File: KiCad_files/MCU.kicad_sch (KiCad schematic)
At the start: 9 parts, among them U1 B3U-1000P, U12 ESP32-S3-MINI-1U

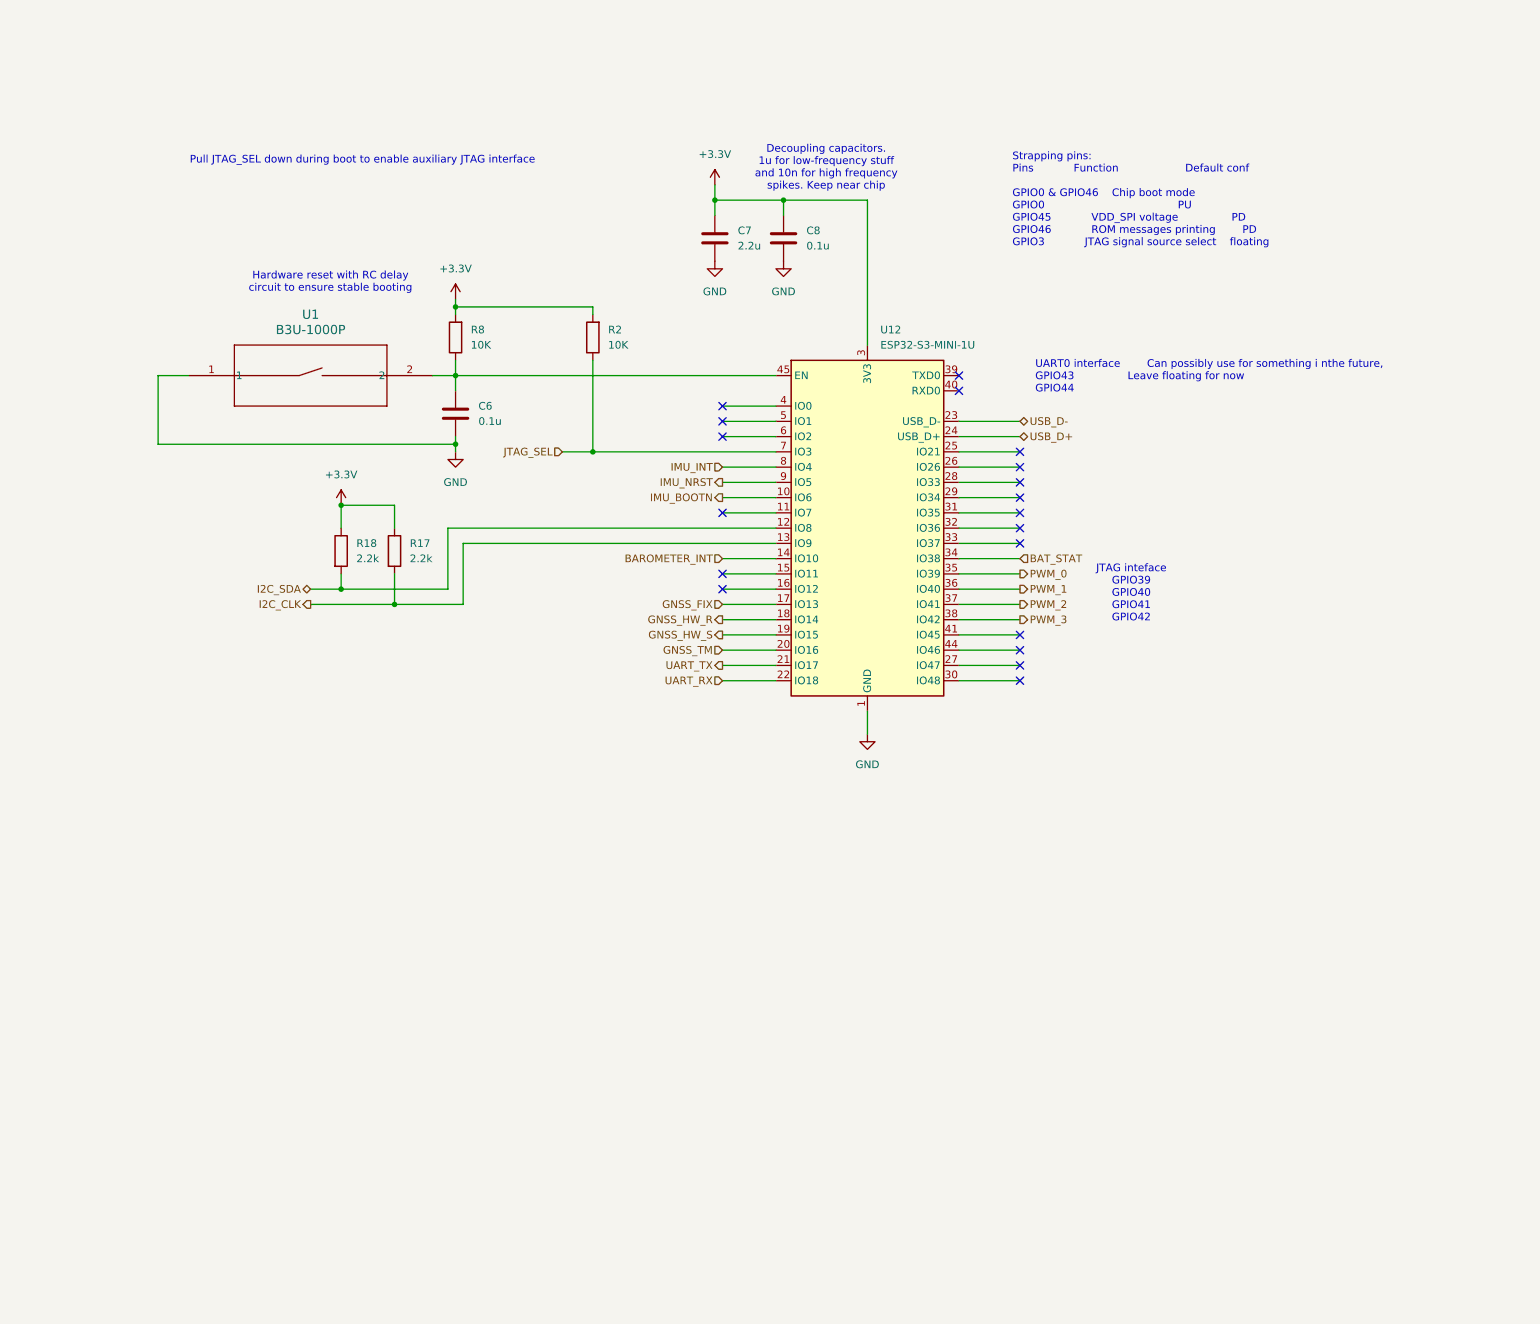
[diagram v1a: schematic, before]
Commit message: headerit mietitty, pinnijärjestystä muutettu mcussa
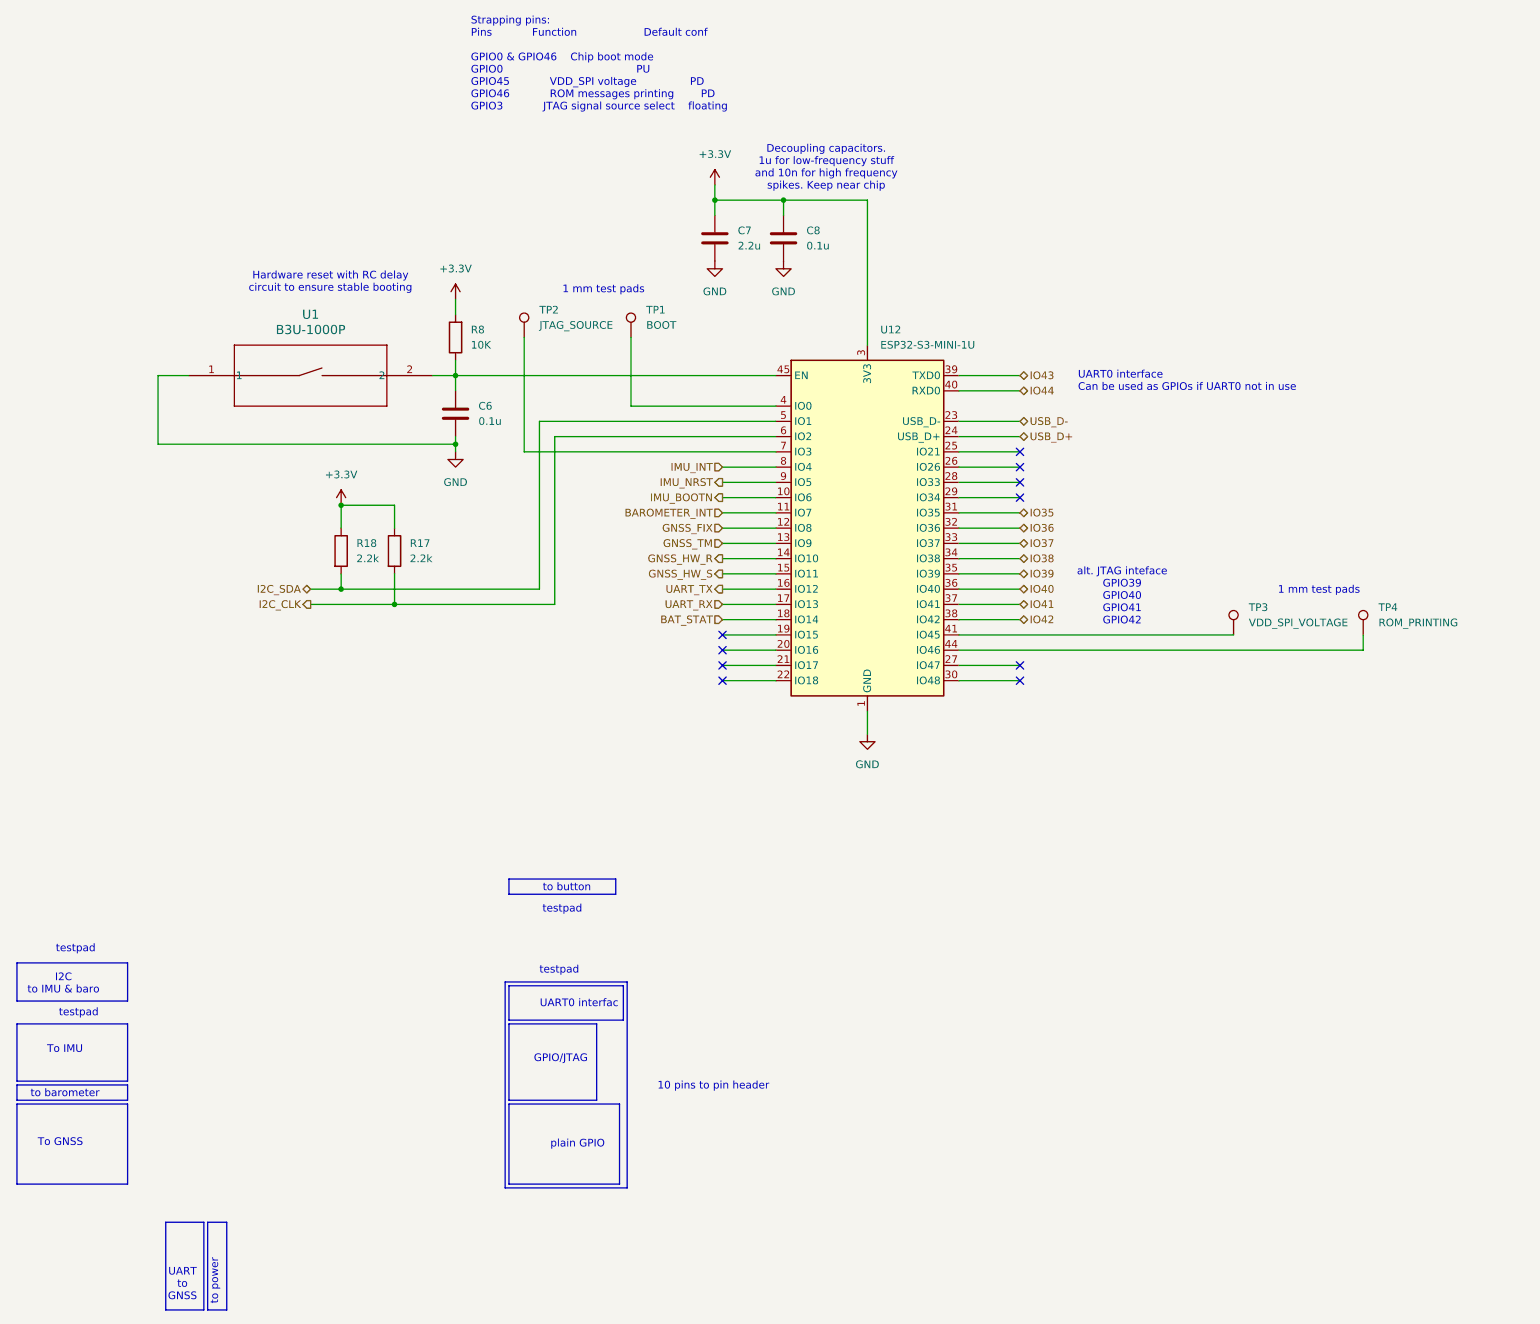
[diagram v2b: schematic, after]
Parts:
- removed R2: 10K, Resistor_SMD:R_0805_2012Metric_Pad1.20x1.40mm_HandSolder, symbol Device:R
- added TP1: BOOT, TestPoint:TestPoint_Pad_D1.0mm, symbol Connector:TestPoint
- added TP2: JTAG_SOURCE, TestPoint:TestPoint_Pad_D1.0mm, symbol Connector:TestPoint
- added TP3: VDD_SPI_VOLTAGE, TestPoint:TestPoint_Pad_D1.0mm, symbol Connector:TestPoint
- added TP4: ROM_PRINTING, TestPoint:TestPoint_Pad_D1.0mm, symbol Connector:TestPoint
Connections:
- net BAROMETER_INT: now also U12.11 (IO7); no longer U12.14 (IO10)
- net BAT_STAT: now also U12.18 (IO14); no longer U12.34 (IO38)
- net GNSS_FIX: now also U12.12 (IO8); no longer U12.17 (IO13)
- net GNSS_HW_R: now also U12.14 (IO10); no longer U12.18 (IO14)
- net GNSS_HW_S: now also U12.15 (IO11); no longer U12.19 (IO15)
- net GNSS_TM: now also U12.13 (IO9); no longer U12.20 (IO16)
- net I2C_CLK: now also U12.6 (IO2); no longer U12.13 (IO9)
- net I2C_SDA: now also U12.5 (IO1); no longer U12.12 (IO8)
- net UART_RX: now also U12.17 (IO13); no longer U12.22 (IO18)
- net UART_TX: now also U12.16 (IO12); no longer U12.21 (IO17)
- net IO35: now reaches U12.31 (IO35)
- net IO36: now reaches U12.32 (IO36)
- net IO37: now reaches U12.33 (IO37)
- net IO43: now reaches U12.39 (TXD0)
- net at U12.4 (IO0): now also TP1.1
- net IO44: now reaches U12.40 (RXD0)
- net at U12.41 (IO45): now also TP3.1
- net at U12.44 (IO46): now also TP4.1
- net JTAG_SEL: no longer names the net of U12.7 (IO3)
- net JTAG_SEL: now also TP2.1
- net PWM_0 renamed IO39
- net PWM_1 renamed IO40
- net PWM_2 renamed IO41
- net PWM_3 renamed IO42
- new net IO38: U12.34 (IO38)
- no-connect marks 19 -> 10
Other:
- note added: "1 mm test pads"
- note added: "10 pins to pin header"
- note added: "GPIO/JTAG"
- note added: "I2C to IMU & baro"
- note added: "To GNSS"
- note added: "To IMU"
- note added: "UART to GNSS"
- note added: "UART0 interfac"
- note added: "UART0 interface Can be used as GPIOs if UART0 not in use"
- note added: "alt. JTAG inteface GPIO39 GPIO40 GPIO41 GPIO42"
- note added: "plain GPIO"
- note added: "testpad"
- note added: "to barometer"
- note added: "to button"
- note added: "to power"
- note removed: "JTAG inteface GPIO39 GPIO40 GPIO41 GPIO42"
- note removed: "Pull JTAG_SEL down during boot to enable auxiliary JTAG interface"
- note removed: "UART0 interface Can possibly use for something i nthe future, GPIO43 Leave floating for now GPIO44"

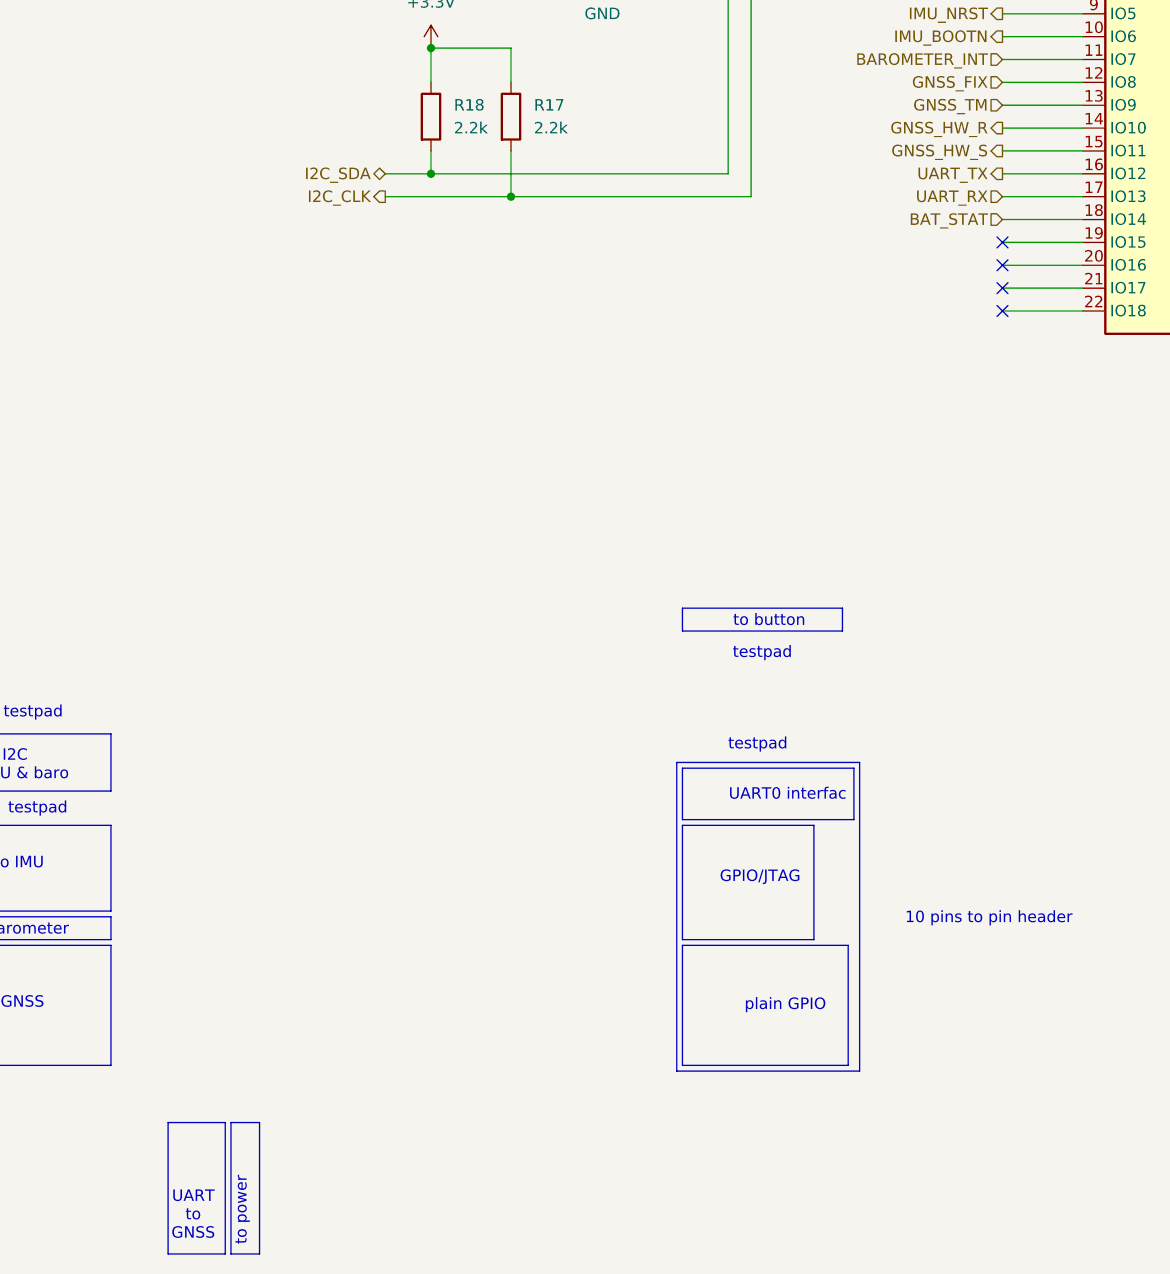
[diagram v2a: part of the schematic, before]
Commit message: UART1 siirretty parempaan paikkaan
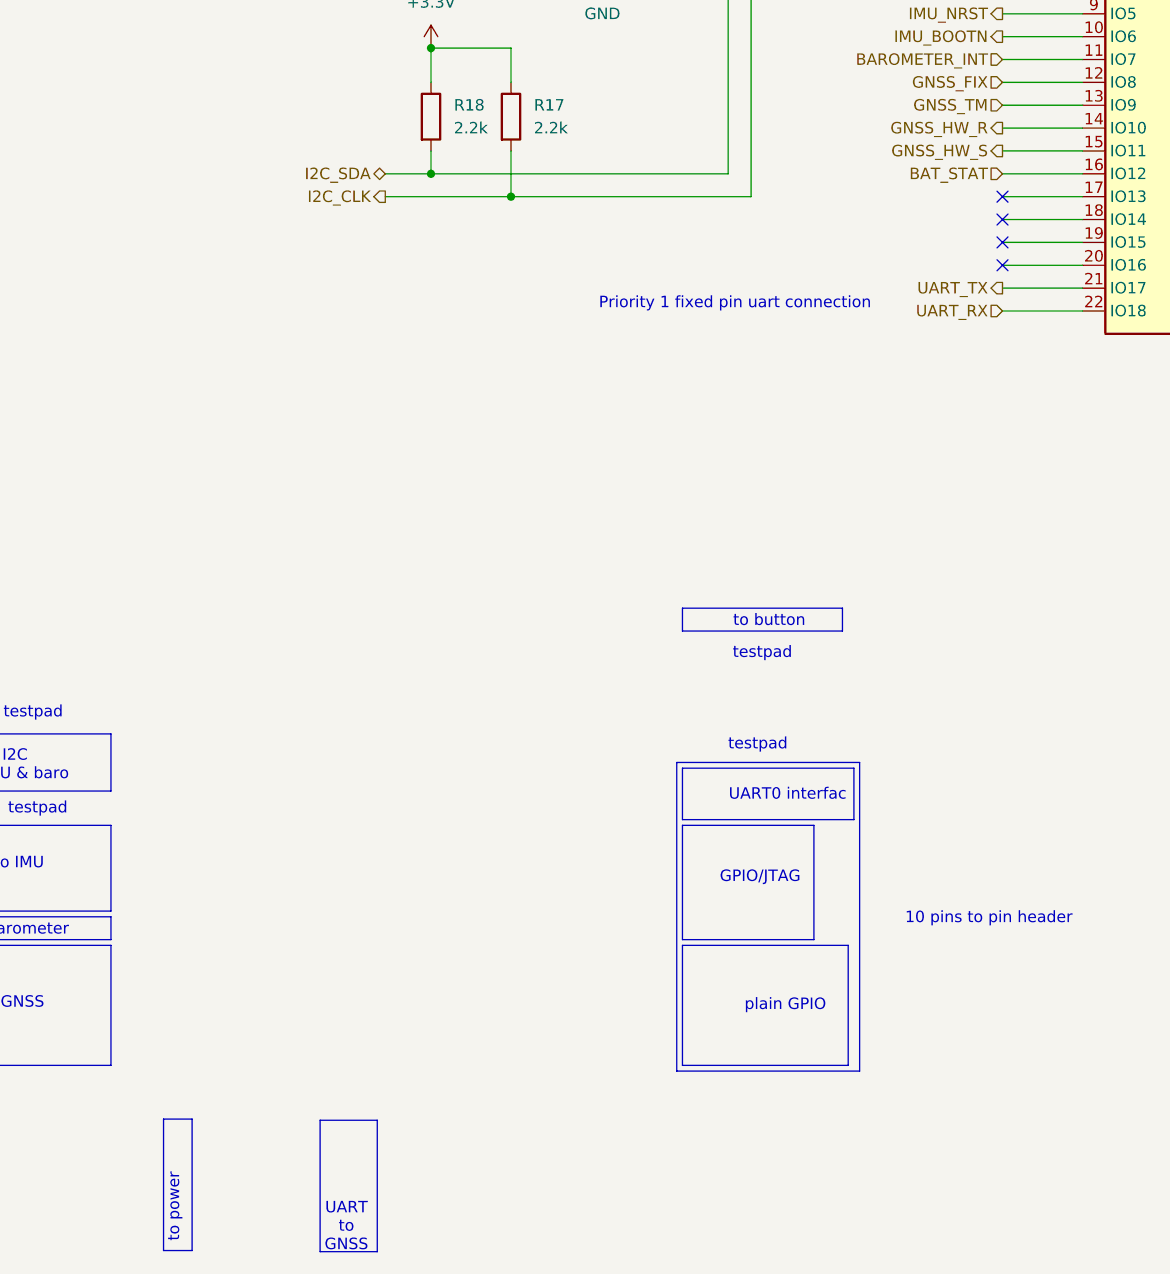
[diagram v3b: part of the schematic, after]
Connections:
- net BAT_STAT: now also U12.16 (IO12); no longer U12.18 (IO14)
- net UART_RX: now also U12.22 (IO18); no longer U12.17 (IO13)
- net UART_TX: now also U12.21 (IO17); no longer U12.16 (IO12)
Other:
- note added: "Priority 1 fixed pin uart connection"
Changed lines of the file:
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@@
 	)
 	(rectangle
-		(start 59.055 220.98)
-		(end 62.23 235.585)
+		(start 51.562 220.599)
+		(end 54.737 235.204)
 		(stroke
 			(width 0)
@@
 	)
 	(rectangle
-		(start 52.07 220.98)
-		(end 58.42 235.585)
+		(start 68.961 220.726)
+		(end 75.311 235.331)
 		(stroke
 			(width 0)
@@
 		)
 	)
+	(text "Priority 1 fixed pin uart connection"
+		(exclude_from_sim no)
+		(at 115.062 130.048 0)
+		(effects
+			(font
+				(size 1.27 1.27)
+			)
+		)
+	)
 	(text "1 mm test pads"
 		(exclude_from_sim no)
@@
 	(text "to power"
 		(exclude_from_sim no)
-		(at 60.198 230.886 90)
+		(at 52.705 230.505 90)
 		(effects
 			(font
@@
 	(text "UART\nto\nGNSS"
 		(exclude_from_sim no)
-		(at 54.864 231.394 0)
+		(at 71.882 232.664 0)
 		(effects
 			(font
@@
 	)
 	(no_connect
-		(at 144.78 123.19)
-	)
-	(no_connect
-		(at 144.78 128.27)
+		(at 144.78 120.65)
 	)
 	(no_connect
@@
 	)
 	(no_connect
+		(at 144.78 123.19)
+	)
+	(no_connect
 		(at 194.31 100.33)
 	)
@@
 	)
 	(no_connect
-		(at 144.78 130.81)
+		(at 144.78 118.11)
 	)
 	(no_connect
@@
 		)
 	)
-	(hierarchical_label "BAT_STAT"
-		(shape input)
-		(at 144.78 120.65 180)
-		(effects
-			(font
-				(size 1.27 1.27)
-			)
-			(justify right)
-		)
-	)
 	(hierarchical_label "GNSS_HW_R"
 		(shape output)
@@
 		)
 	)
+	(hierarchical_label "UART_RX"
+		(shape input)
+		(at 144.78 130.81 180)
+		(effects
+			(font
+				(size 1.27 1.27)
+			)
+			(justify right)
+		)
+	)
 	(hierarchical_label "GNSS_TM"
 		(shape input)
@@
 		)
 	)
-	(hierarchical_label "UART_TX"
-		(shape output)
+	(hierarchical_label "BAT_STAT"
+		(shape input)
 		(at 144.78 115.57 180)
-		(effects
-			(font
-				(size 1.27 1.27)
-			)
-			(justify right)
-		)
-	)
-	(hierarchical_label "UART_RX"
-		(shape input)
-		(at 144.78 118.11 180)
 		(effects
 			(font
@@
 		)
 	)
+	(hierarchical_label "UART_TX"
+		(shape output)
+		(at 144.78 128.27 180)
+		(effects
+			(font
+				(size 1.27 1.27)
+			)
+			(justify right)
+		)
+	)

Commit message: gepsiä alotettu
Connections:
- net BAT_STAT: now also U12.30 (IO48); no longer U12.16 (IO12)
- net GNSS_FIX: now also U12.18 (IO14); no longer U12.12 (IO8)
- net GNSS_HW_R: now also U12.20 (IO16); no longer U12.14 (IO10)
- net GNSS_HW_S: now also U12.17 (IO13); no longer U12.15 (IO11)
- net GNSS_TM: now also U12.19 (IO15); no longer U12.13 (IO9)
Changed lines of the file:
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@@
 	)
 	(no_connect
-		(at 144.78 125.73)
+		(at 144.78 107.95)
 	)
 	(no_connect
-		(at 144.78 120.65)
+		(at 144.78 115.57)
+	)
+	(no_connect
+		(at 144.78 113.03)
 	)
 	(no_connect
@@
 	)
 	(no_connect
-		(at 144.78 123.19)
-	)
-	(no_connect
 		(at 194.31 100.33)
 	)
@@
 	)
 	(no_connect
+		(at 144.78 110.49)
+	)
+	(no_connect
+		(at 144.78 105.41)
+	)
+	(no_connect
 		(at 194.31 97.79)
-	)
-	(no_connect
-		(at 144.78 118.11)
-	)
-	(no_connect
-		(at 194.31 130.81)
 	)
 	(wire
@@
 		)
 	)
+	(hierarchical_label "GNSS_TM"
+		(shape input)
+		(at 144.78 123.19 180)
+		(effects
+			(font
+				(size 1.27 1.27)
+			)
+			(justify right)
+		)
+	)
 	(hierarchical_label "IO39"
 		(shape bidirectional)
@@
 		)
 	)
-	(hierarchical_label "GNSS_HW_R"
-		(shape output)
-		(at 144.78 110.49 180)
-		(effects
-			(font
-				(size 1.27 1.27)
-			)
-			(justify right)
-		)
-	)
 	(hierarchical_label "IO36"
 		(shape bidirectional)
@@
 		)
 	)
-	(hierarchical_label "GNSS_FIX"
-		(shape input)
-		(at 144.78 105.41 180)
-		(effects
-			(font
-				(size 1.27 1.27)
-			)
-			(justify right)
-		)
-	)
 	(hierarchical_label "IMU_BOOTN"
 		(shape output)
@@
 		)
 	)
+	(hierarchical_label "BAT_STAT"
+		(shape input)
+		(at 194.31 130.81 0)
+		(effects
+			(font
+				(size 1.27 1.27)
+			)
+			(justify left)
+		)
+	)
 	(hierarchical_label "IO38"
 		(shape bidirectional)
@@
 		)
 	)
+	(hierarchical_label "GNSS_HW_R"
+		(shape output)
+		(at 144.78 125.73 180)
+		(effects
+			(font
+				(size 1.27 1.27)
+			)
+			(justify right)
+		)
+	)
 	(hierarchical_label "IO42"
 		(shape bidirectional)
@@
 		)
 	)
+	(hierarchical_label "GNSS_FIX"
+		(shape input)
+		(at 144.78 120.65 180)
+		(effects
+			(font
+				(size 1.27 1.27)
+			)
+			(justify right)
+		)
+	)
 	(hierarchical_label "USB_D-"
 		(shape bidirectional)
@@
 		)
 	)
-	(hierarchical_label "GNSS_TM"
-		(shape input)
-		(at 144.78 107.95 180)
-		(effects
-			(font
-				(size 1.27 1.27)
-			)
-			(justify right)
-		)
-	)
-	(hierarchical_label "GNSS_HW_S"
-		(shape output)
-		(at 144.78 113.03 180)
-		(effects
-			(font
-				(size 1.27 1.27)
-			)
-			(justify right)
-		)
-	)
 	(hierarchical_label "IO37"
 		(shape bidirectional)
@@
 		)
 	)
-	(hierarchical_label "BAT_STAT"
-		(shape input)
-		(at 144.78 115.57 180)
-		(effects
-			(font
-				(size 1.27 1.27)
-			)
-			(justify right)
-		)
-	)
 	(hierarchical_label "IO40"
 		(shape bidirectional)
@@
 		)
 	)
+	(hierarchical_label "GNSS_HW_S"
+		(shape output)
+		(at 144.78 118.11 180)
+		(effects
+			(font
+				(size 1.27 1.27)
+			)
+			(justify right)
+		)
+	)
